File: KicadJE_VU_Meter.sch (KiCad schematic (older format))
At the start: 63 parts, among them J1 Out, J2 In1, J3 In2, J4 Out, P1 HEADER_2x5_Doepfer, U1 TL072

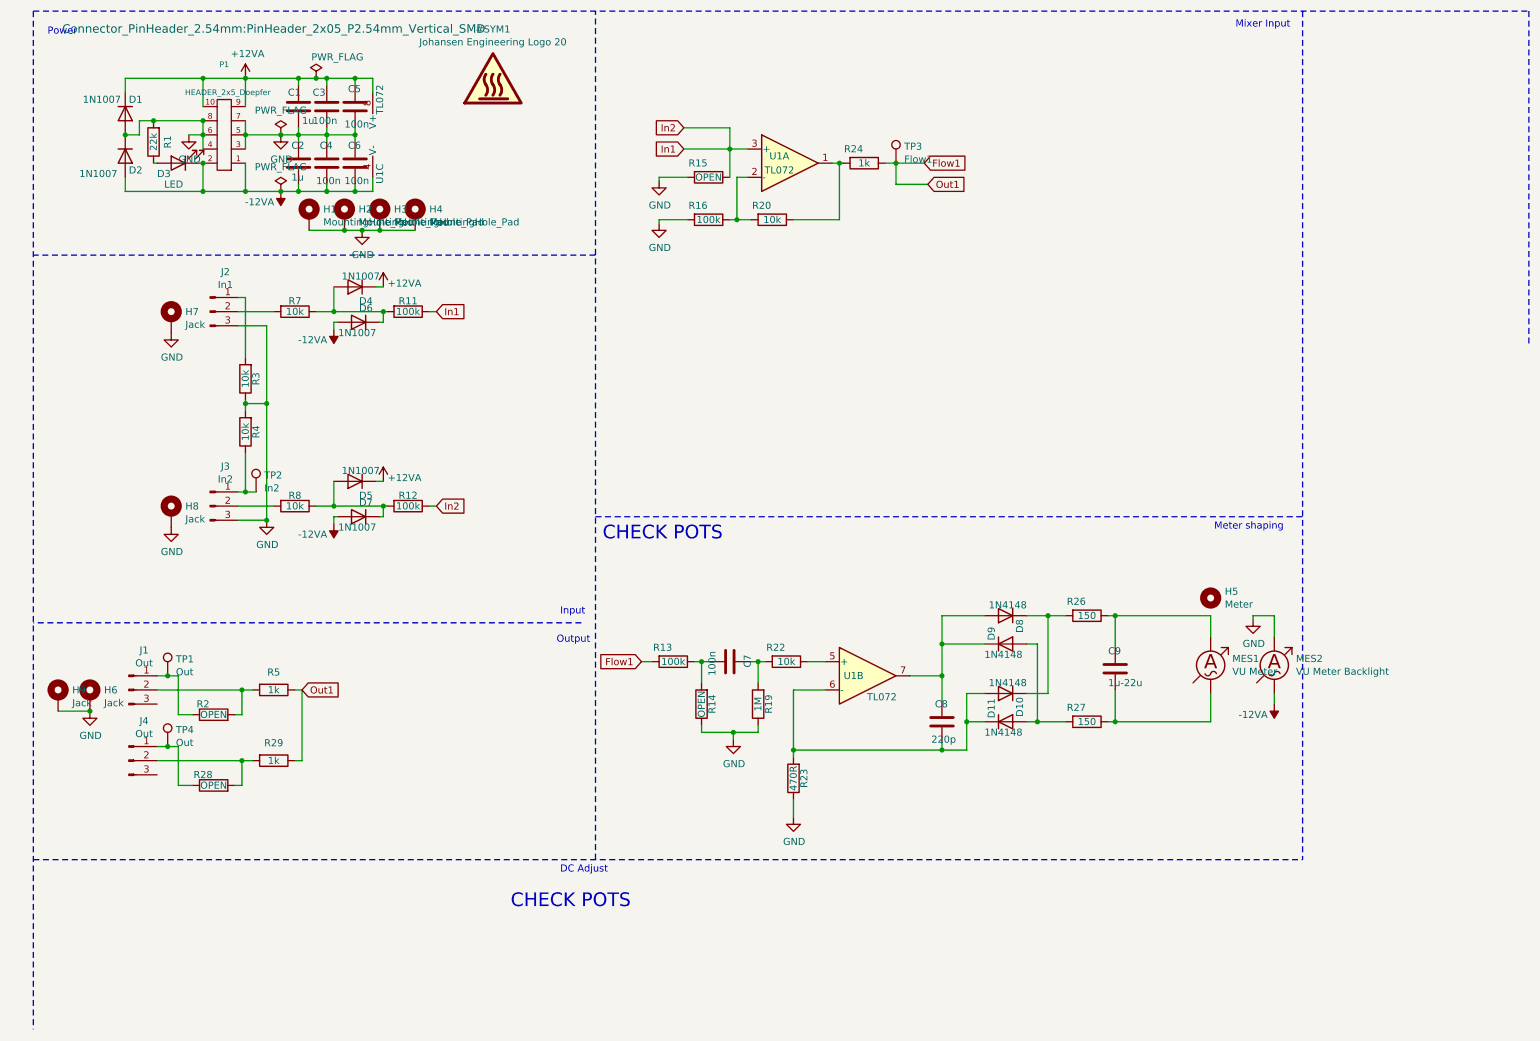
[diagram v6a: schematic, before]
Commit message: Adjusting labels
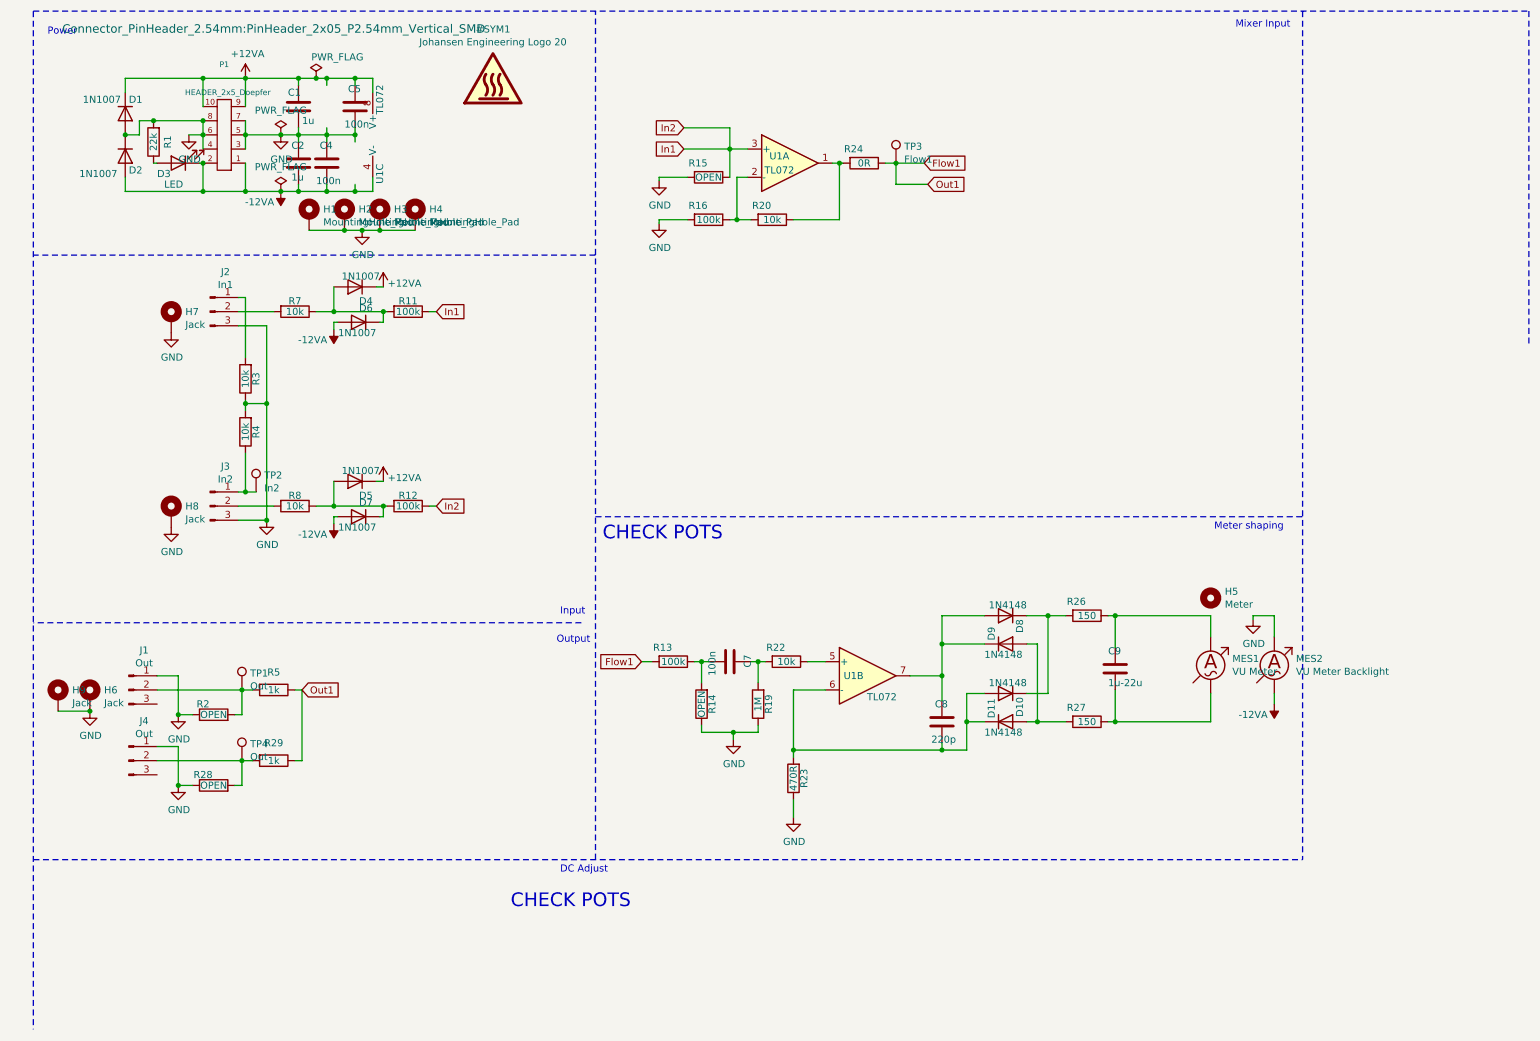
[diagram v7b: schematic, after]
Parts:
- removed C3, C6: 100n, Capacitor_SMD:C_0805_2012Metric, symbol Device:C
- R24: value 1k -> 0R
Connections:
- net GND: now also J1.1 (Pin_1), J4.1 (Pin_1), R2.1, R28.1
- net at J1.2 (Pin_2), R2.2, R5.2: now also TP1.1
- net at J4.2 (Pin_2), R28.2, R29.2: now also TP4.1
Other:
- moved on the sheet: TP1, TP4
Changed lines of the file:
@@
 $EndDescr
-Wire Wire Line
-	1550 5225 1475 5225
 Wire Wire Line
 	1975 4025 2225 4025
@@
 F 3 "" H 1625 1400 50  0001 C CNN
 	1    1625 1400
-	1    0    0    -1
-$EndComp
-$Comp
-L Device:C C?
-U 1 1 5F4F8A7C
-P 2600 1200
-AR Path="/5E4B0DD9/5F4F8A7C" Ref="C?"  Part="1"
-AR Path="/5E62ACA1/5F4F8A7C" Ref="C?"  Part="1"
-AR Path="/5F49A670/5F4F8A7C" Ref="C?"  Part="1"
-AR Path="/5F4F8A7C" Ref="C3"  Part="1"
-F 0 "C3" H 2500 1300 50  0000 L CNN
-F 1 "100n" H 2500 1100 50  0000 L CNN
-F 2 "Capacitor_SMD:C_0805_2012Metric" H 2638 1050 50  0001 C CNN
-F 3 "~" H 2600 1200 50  0001 C CNN
-	1    2600 1200
 	1    0    0    -1
 $EndComp
@@
 Text Notes 4225 5000 0    50   ~ 0
 Output
-$Comp
-L Device:C C?
-U 1 1 5EA5FADA
-P 2800 1600
-AR Path="/5E4B0DD9/5EA5FADA" Ref="C?"  Part="1"
-AR Path="/5E62ACA1/5EA5FADA" Ref="C?"  Part="1"
-AR Path="/5F49A670/5EA5FADA" Ref="C?"  Part="1"
-AR Path="/5EA5FADA" Ref="C6"  Part="1"
-F 0 "C6" H 2750 1725 50  0000 L CNN
-F 1 "100n" H 2725 1475 50  0000 L CNN
-F 2 "Capacitor_SMD:C_0805_2012Metric" H 2838 1450 50  0001 C CNN
-F 3 "~" H 2800 1600 50  0001 C CNN
-	1    2800 1600
-	1    0    0    -1
-$EndComp
 Wire Wire Line
 	2800 1450 2800 1400
@@
 L Connector:TestPoint TP1
 U 1 1 5EE75A89
-P 1475 5225
-F 0 "TP1" H 1533 5343 50  0000 L CNN
-F 1 "Out" H 1533 5252 50  0000 L CNN
-F 2 "TestPoint:TestPoint_Pad_D2.0mm" H 1675 5225 50  0001 C CNN
-F 3 "~" H 1675 5225 50  0001 C CNN
-	1    1475 5225
-	1    0    0    -1
-$EndComp
-Connection ~ 1475 5225
-Wire Wire Line
-	1475 5225 1400 5225
+P 2000 5325
+F 0 "TP1" H 2058 5443 50  0000 L CNN
+F 1 "Out" H 2058 5352 50  0000 L CNN
+F 2 "TestPoint:TestPoint_Pad_D2.0mm" H 2200 5325 50  0001 C CNN
+F 3 "~" H 2200 5325 50  0001 C CNN
+	1    2000 5325
+	1    0    0    -1
+$EndComp
 $Comp
 L Connector:TestPoint TP2
@@
 AR Path="/5F49A670/5F90A421" Ref="R?"  Part="1"
 F 0 "R24" V 6300 1525 50  0000 C CNN
-F 1 "1k" V 6400 1600 50  0000 C CNN
+F 1 "0R" V 6400 1600 50  0000 C CNN
 F 2 "Resistor_SMD:R_0805_2012Metric_Pad1.20x1.40mm_HandSolder" V 6330 1600 50  0001 C CNN
 F 3 "~" H 6400 1600 50  0001 C CNN
@@
 Connection ~ 925  5475
 Wire Wire Line
-	1550 5725 1475 5725
-Wire Wire Line
 	2375 5825 2425 5825
 $Comp
@@
 L Connector:TestPoint TP4
 U 1 1 60AFA9F0
-P 1475 5725
-F 0 "TP4" H 1533 5843 50  0000 L CNN
-F 1 "Out" H 1533 5752 50  0000 L CNN
-F 2 "TestPoint:TestPoint_Pad_D2.0mm" H 1675 5725 50  0001 C CNN
-F 3 "~" H 1675 5725 50  0001 C CNN
-	1    1475 5725
-	1    0    0    -1
-$EndComp
-Connection ~ 1475 5725
-Wire Wire Line
-	1475 5725 1400 5725
+P 2000 5825
+F 0 "TP4" H 2058 5943 50  0000 L CNN
+F 1 "Out" H 2058 5852 50  0000 L CNN
+F 2 "TestPoint:TestPoint_Pad_D2.0mm" H 2200 5825 50  0001 C CNN
+F 3 "~" H 2200 5825 50  0001 C CNN
+	1    2000 5825
+	1    0    0    -1
+$EndComp
 $Comp
 L Device:R R28
@@
 Wire Wire Line
 	2000 6000 2000 5825
-Wire Wire Line
-	1400 5825 2000 5825
 Connection ~ 2000 5825
 Wire Wire Line
@@
 Wire Wire Line
 	5450 1350 5125 1350
+Wire Wire Line
+	1400 5725 1550 5725
+Wire Wire Line
+	1400 5825 2000 5825
+Wire Wire Line
+	1400 5225 1550 5225
+$Comp
+L KicadJE_VU_Meter-rescue:GND-Envelope-cache-2018-08-04-13-00-04-KicadJE_Util-rescue #PWR0106
+U 1 1 60D60E18
+P 1550 5500
+AR Path="/60D60E18" Ref="#PWR0106"  Part="1"
+AR Path="/5C8C5FC0/60D60E18" Ref="#PWR?"  Part="1"
+AR Path="/5CAAE8D3/60D60E18" Ref="#PWR?"  Part="1"
+AR Path="/5E4B0DD9/60D60E18" Ref="#PWR?"  Part="1"
+AR Path="/5E62ACA1/60D60E18" Ref="#PWR?"  Part="1"
+AR Path="/5F49A670/60D60E18" Ref="#PWR?"  Part="1"
+F 0 "#PWR0106" H 1550 5250 50  0001 C CNN
+F 1 "GND" H 1555 5327 50  0000 C CNN
+F 2 "" H 1550 5500 50  0001 C CNN
+F 3 "" H 1550 5500 50  0001 C CNN
+	1    1550 5500
+	1    0    0    -1
+$EndComp
+Connection ~ 1550 5500
+$Comp
+L KicadJE_VU_Meter-rescue:GND-Envelope-cache-2018-08-04-13-00-04-KicadJE_Util-rescue #PWR0107
+U 1 1 60D611C1
+P 1550 6000
+AR Path="/60D611C1" Ref="#PWR0107"  Part="1"
+AR Path="/5C8C5FC0/60D611C1" Ref="#PWR?"  Part="1"
+AR Path="/5CAAE8D3/60D611C1" Ref="#PWR?"  Part="1"
+AR Path="/5E4B0DD9/60D611C1" Ref="#PWR?"  Part="1"
+AR Path="/5E62ACA1/60D611C1" Ref="#PWR?"  Part="1"
+AR Path="/5F49A670/60D611C1" Ref="#PWR?"  Part="1"
+F 0 "#PWR0107" H 1550 5750 50  0001 C CNN
+F 1 "GND" H 1555 5827 50  0000 C CNN
+F 2 "" H 1550 6000 50  0001 C CNN
+F 3 "" H 1550 6000 50  0001 C CNN
+	1    1550 6000
+	1    0    0    -1
+$EndComp
+Connection ~ 1550 6000
 $EndSCHEMATC
